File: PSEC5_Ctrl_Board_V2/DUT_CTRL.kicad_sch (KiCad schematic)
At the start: 2 parts, among them J2 QSH-040-01-X-D-DP-A, J4 QSH-040-01-X-D-DP-A

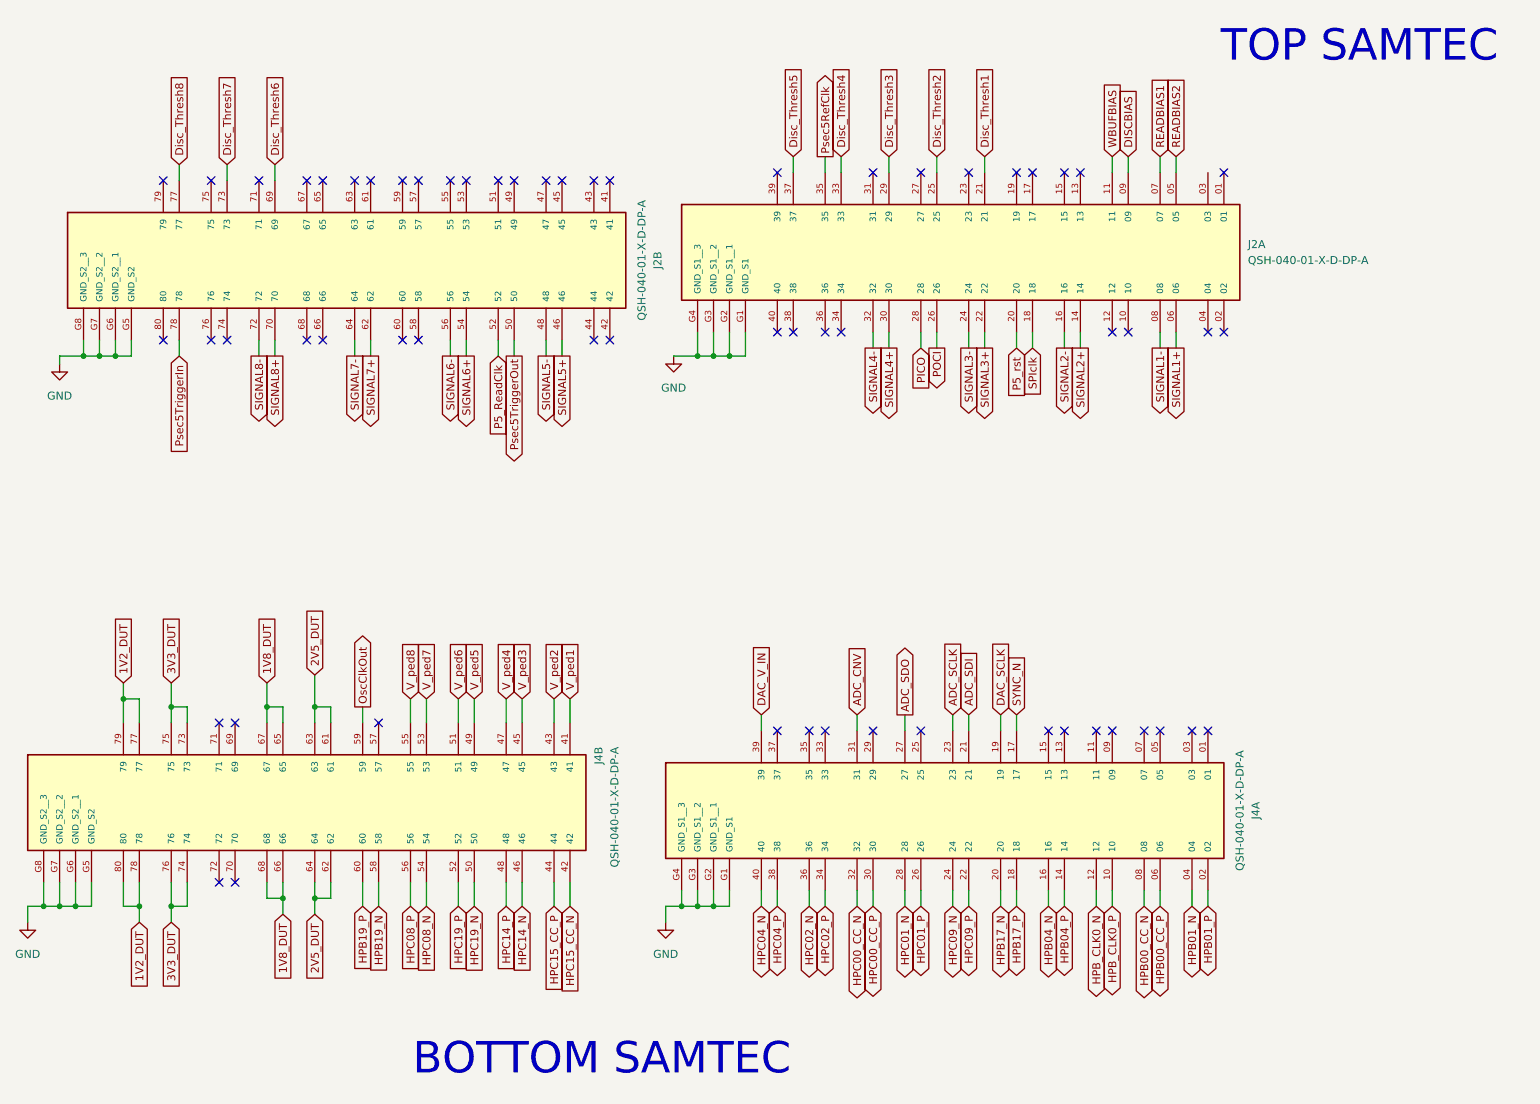
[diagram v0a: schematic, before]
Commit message: Updated V2
New Power Planes, roruing of bottom samtec and kria positions
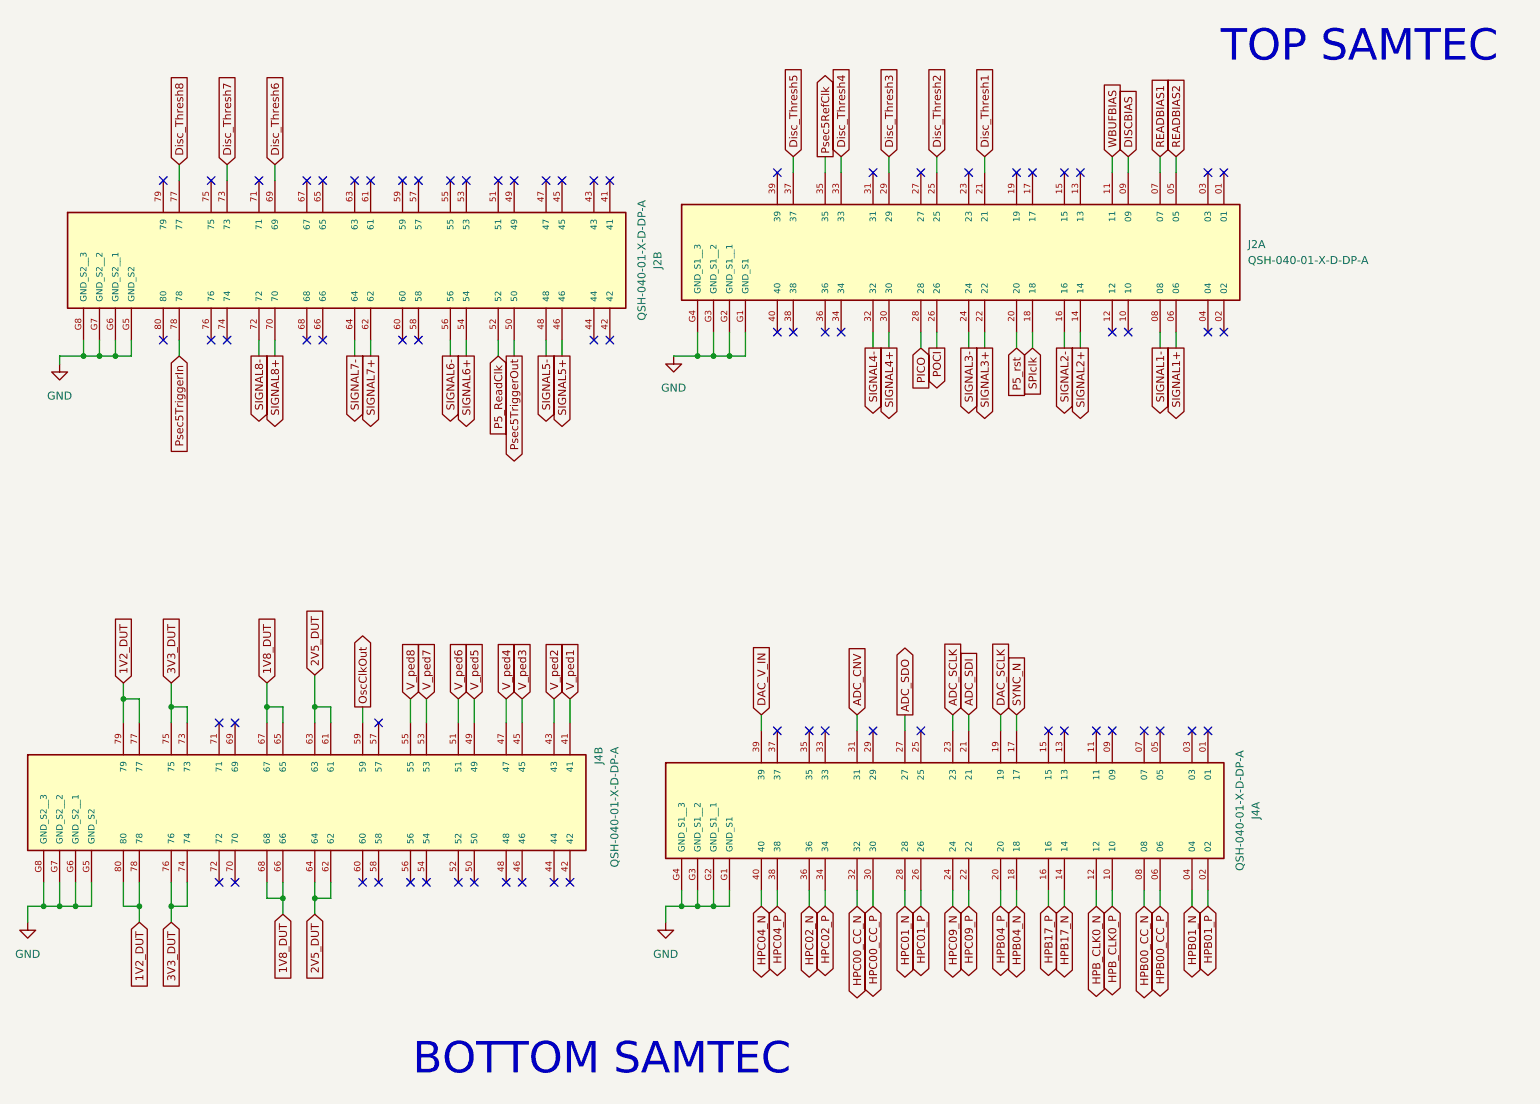
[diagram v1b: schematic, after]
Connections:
- net HPB04_N: now also J4.18; no longer J4.16
- net HPB04_P: now also J4.20; no longer J4.14
- net HPB17_N: now also J4.14; no longer J4.20
- net HPB17_P: now also J4.16; no longer J4.18
- net HPB19_N: no longer names the net of J4.58
- net HPB19_P: no longer names the net of J4.60
- net HPC08_N: no longer names the net of J4.54
- net HPC08_P: no longer names the net of J4.56
- net HPC14_N: no longer names the net of J4.46
- net HPC14_P: no longer names the net of J4.48
- net HPC15_CC_N: no longer names the net of J4.42
- net HPC15_CC_P: no longer names the net of J4.44
- net HPC19_N: no longer names the net of J4.50
- net HPC19_P: no longer names the net of J4.52
- no-connect marks 61 -> 72
